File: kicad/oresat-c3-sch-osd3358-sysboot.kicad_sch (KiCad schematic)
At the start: 21 parts, among them J6 Conn_01x02, U1 OSD3358-512M-BSM

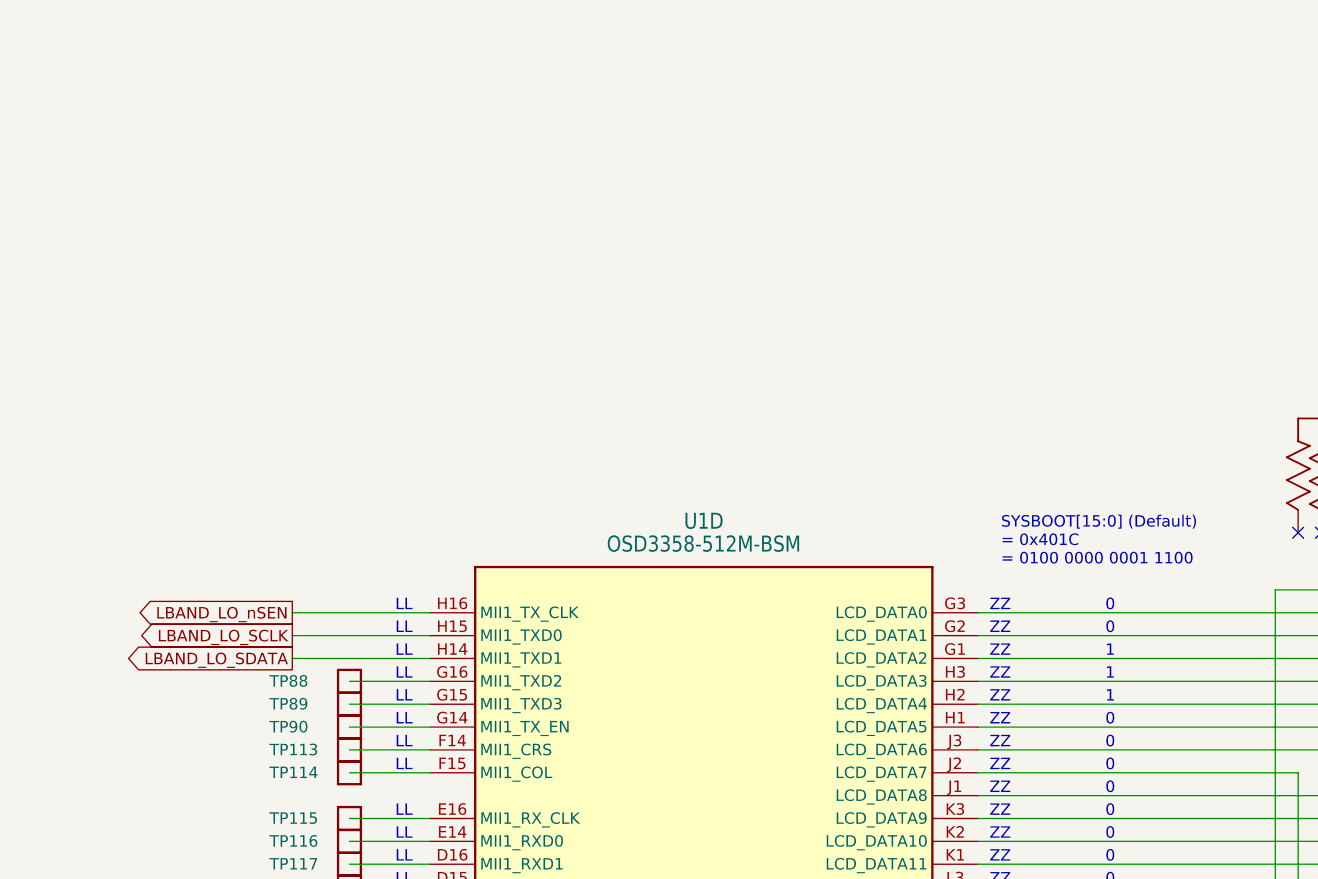
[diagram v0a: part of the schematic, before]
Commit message: Ryan made me do it: added CAN0 tranceiver.
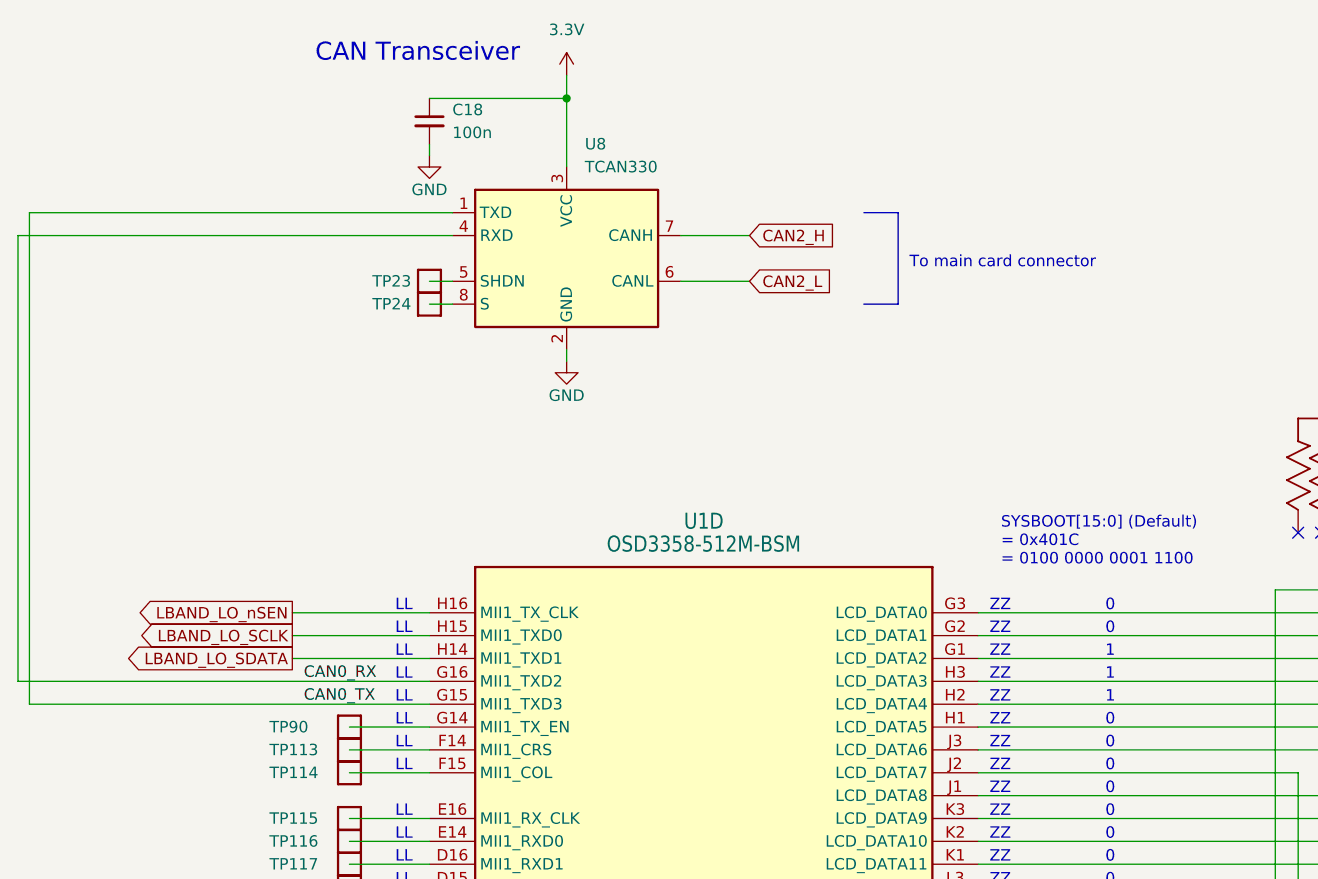
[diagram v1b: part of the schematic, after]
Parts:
- removed TP88, TP89: Test-Point, oresat-misc:TestPoint_Pad_D1.0mm, symbol oresat-misc:Test-Point-1mm-round
- added C18: 100n, Capacitor_SMD:C_0603_1608Metric, symbol Device:C_Small
- added TP23, TP24: Test-Point, oresat-misc:TestPoint_Pad_D1.0mm, symbol oresat-misc:Test-Point-1mm-round
- added U8: TCAN330, Package_TO_SOT_SMD:SOT-23-8, symbol Interface_CAN_LIN:TCAN330
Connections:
- net 3.3V: now also C18.1, U8.3 (VCC)
- net GND: now also C18.2, U8.2 (GND)
- net CAN0_TX: now reaches U1.G15 (MII1_TXD3)
- net CAN0_TX: now also U8.1 (TXD)
- net CAN0_RX: now reaches U1.G16 (MII1_TXD2)
- net CAN0_RX: now also U8.4 (RXD)
- new net: TP23.1, U8.5 (SHDN)
- new net: TP24.1, U8.8 (S)
- new net CAN2_H: U8.7 (CANH)
- new net CAN2_L: U8.6 (CANL)
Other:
- note added: "CAN Transceiver"
- note added: "To main card connector"

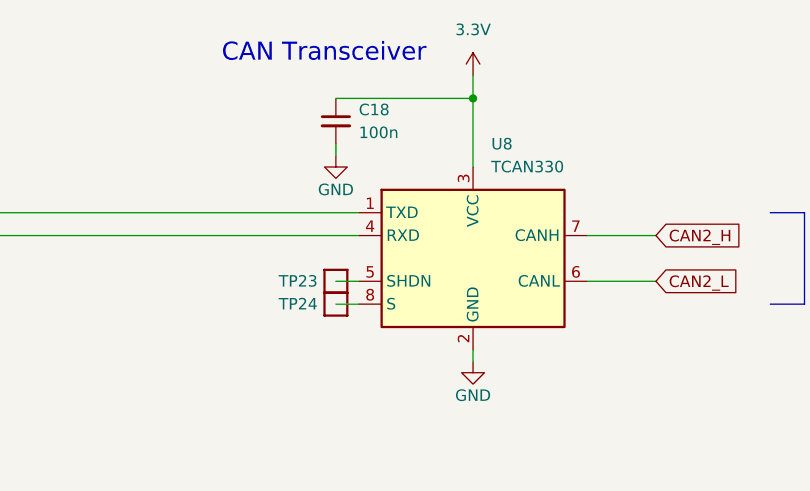
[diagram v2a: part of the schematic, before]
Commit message: Fixed Q1 in the I2C subsystem, which was backward but we never noticed. Removed hardware ID resistors and added back in test points, since HW ID is now stored in internal EEPROM. Updated power measurement values in UHF transmit path. Finally, added circuitry to enable USB lines over the UART backplane. This involves switching the UART signals for the USB signals, and pulling VBUS high to trigger USB on the Octavo. It's pretty janky, so we'll see if it works!
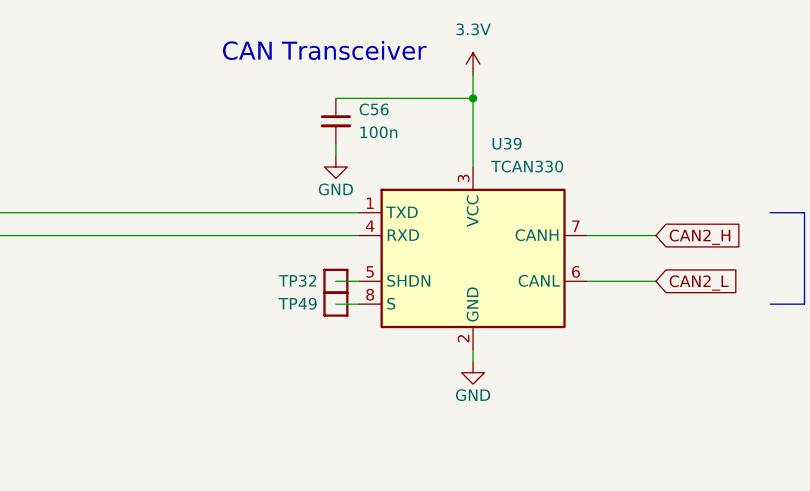
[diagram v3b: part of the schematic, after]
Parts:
- renumbered C18 to C56, TP23 to TP32, TP24 to TP49, U8 to U39
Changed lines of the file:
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@@
   (symbol (lib_id "oresat-power:3.3V") (at 132.08 69.85 0) (unit 1)
     (in_bom yes) (on_board yes) (dnp no) (fields_autoplaced)
-    (property "Reference" "#3V0105" (at 132.08 73.66 0)
+    (property "Reference" "#3V06" (at 132.08 73.66 0)
       (effects (font (size 1.27 1.27)) hide)
     )
@@
     (instances
       (project "oresat-c3"
-        (path "/65d12cdd-c326-4033-9053-c59fa4e0b25e/f3d147ad-4cea-4d77-ae60-95882b03454e"
-          (reference "#3V0105") (unit 1)
-        )
         (path "/65d12cdd-c326-4033-9053-c59fa4e0b25e/0c732c1e-ab0d-41ac-9d77-9d7763333b6f"
           (reference "#3V06") (unit 1)
@@
   (symbol (lib_id "Interface_CAN_LIN:TCAN330") (at 132.08 90.17 0) (unit 1)
     (in_bom yes) (on_board yes) (dnp no) (fields_autoplaced)
-    (property "Reference" "U8" (at 134.0994 77.47 0)
+    (property "Reference" "U39" (at 134.0994 77.47 0)
       (effects (font (size 1.27 1.27)) (justify left))
     )
@@
     (instances
       (project "oresat-c3"
-        (path "/65d12cdd-c326-4033-9053-c59fa4e0b25e/f3d147ad-4cea-4d77-ae60-95882b03454e"
-          (reference "U8") (unit 1)
-        )
         (path "/65d12cdd-c326-4033-9053-c59fa4e0b25e/0c732c1e-ab0d-41ac-9d77-9d7763333b6f"
           (reference "U39") (unit 1)
@@
   (symbol (lib_id "oresat-misc:Test-Point-1mm-round") (at 116.84 92.71 0) (unit 1)
     (in_bom yes) (on_board yes) (dnp no)
-    (property "Reference" "TP23" (at 110.49 92.71 0)
+    (property "Reference" "TP32" (at 110.49 92.71 0)
       (effects (font (size 1.27 1.27)) (justify left))
     )
@@
     (instances
       (project "oresat-c3"
-        (path "/65d12cdd-c326-4033-9053-c59fa4e0b25e/f3d147ad-4cea-4d77-ae60-95882b03454e"
-          (reference "TP23") (unit 1)
-        )
         (path "/65d12cdd-c326-4033-9053-c59fa4e0b25e/0c732c1e-ab0d-41ac-9d77-9d7763333b6f"
           (reference "TP32") (unit 1)
@@
   (symbol (lib_id "Device:C_Small") (at 116.84 74.93 0) (unit 1)
     (in_bom yes) (on_board yes) (dnp no) (fields_autoplaced)
-    (property "Reference" "C18" (at 119.38 73.6662 0)
+    (property "Reference" "C56" (at 119.38 73.6662 0)
       (effects (font (size 1.27 1.27)) (justify left))
     )
@@
     (instances
       (project "oresat-c3"
-        (path "/65d12cdd-c326-4033-9053-c59fa4e0b25e/f3d147ad-4cea-4d77-ae60-95882b03454e"
-          (reference "C18") (unit 1)
-        )
         (path "/65d12cdd-c326-4033-9053-c59fa4e0b25e/0c732c1e-ab0d-41ac-9d77-9d7763333b6f"
           (reference "C56") (unit 1)
@@
   (symbol (lib_id "oresat-misc:Test-Point-1mm-round") (at 116.84 95.25 0) (unit 1)
     (in_bom yes) (on_board yes) (dnp no)
-    (property "Reference" "TP24" (at 110.49 95.25 0)
+    (property "Reference" "TP49" (at 110.49 95.25 0)
       (effects (font (size 1.27 1.27)) (justify left))
     )
@@
     (instances
       (project "oresat-c3"
-        (path "/65d12cdd-c326-4033-9053-c59fa4e0b25e/f3d147ad-4cea-4d77-ae60-95882b03454e"
-          (reference "TP24") (unit 1)
-        )
         (path "/65d12cdd-c326-4033-9053-c59fa4e0b25e/0c732c1e-ab0d-41ac-9d77-9d7763333b6f"
           (reference "TP49") (unit 1)
@@
   (symbol (lib_id "power:GND") (at 132.08 101.6 0) (unit 1)
     (in_bom yes) (on_board yes) (dnp no)
-    (property "Reference" "#PWR0159" (at 132.08 107.95 0)
+    (property "Reference" "#PWR014" (at 132.08 107.95 0)
       (effects (font (size 1.27 1.27)) hide)
     )
@@
     (instances
       (project "oresat-c3"
-        (path "/65d12cdd-c326-4033-9053-c59fa4e0b25e/f3d147ad-4cea-4d77-ae60-95882b03454e"
-          (reference "#PWR0159") (unit 1)
-        )
         (path "/65d12cdd-c326-4033-9053-c59fa4e0b25e/0c732c1e-ab0d-41ac-9d77-9d7763333b6f"
           (reference "#PWR014") (unit 1)
@@
   (symbol (lib_id "power:GND") (at 116.84 78.74 0) (unit 1)
     (in_bom yes) (on_board yes) (dnp no)
-    (property "Reference" "#PWR0156" (at 116.84 85.09 0)
+    (property "Reference" "#PWR013" (at 116.84 85.09 0)
       (effects (font (size 1.27 1.27)) hide)
     )
@@
     (instances
       (project "oresat-c3"
-        (path "/65d12cdd-c326-4033-9053-c59fa4e0b25e/f3d147ad-4cea-4d77-ae60-95882b03454e"
-          (reference "#PWR0156") (unit 1)
-        )
         (path "/65d12cdd-c326-4033-9053-c59fa4e0b25e/0c732c1e-ab0d-41ac-9d77-9d7763333b6f"
           (reference "#PWR013") (unit 1)

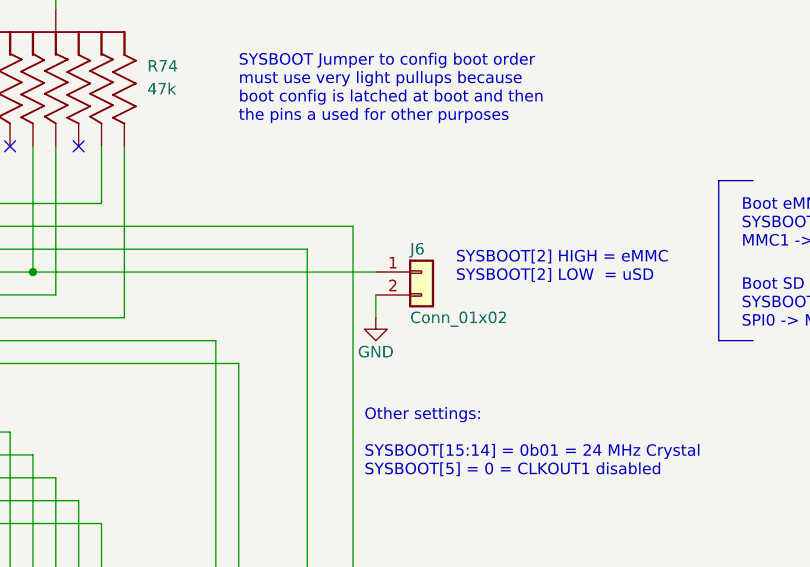
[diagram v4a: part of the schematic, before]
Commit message: BOM cleanups; modified test points to not show up on BOMs, fixed some minor BOM shenaigans (3k vs 3.0k), and imported into the board.
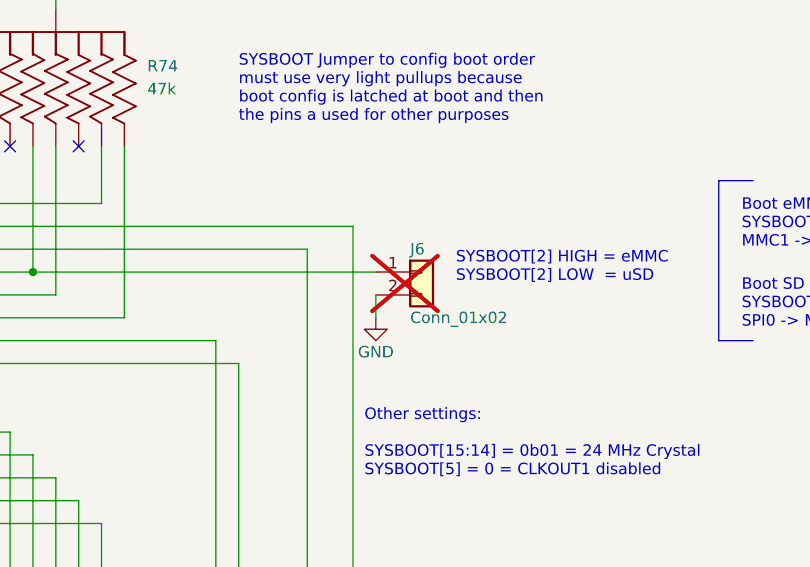
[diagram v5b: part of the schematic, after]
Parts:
- J6: now not fitted
- TP113, TP114, TP115, TP116, TP117, TP118, TP119, TP120, TP121, TP123, TP125, TP134, TP136, TP32, TP49, TP90: now left out of the parts list

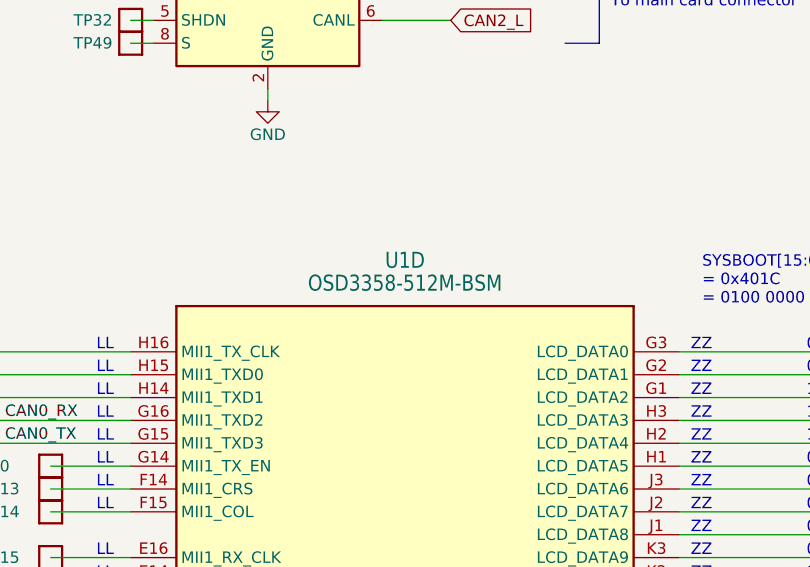
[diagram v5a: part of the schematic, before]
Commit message: Fixed more part numbers while in process of doing BOM inventory, including eMMC and FRAM.
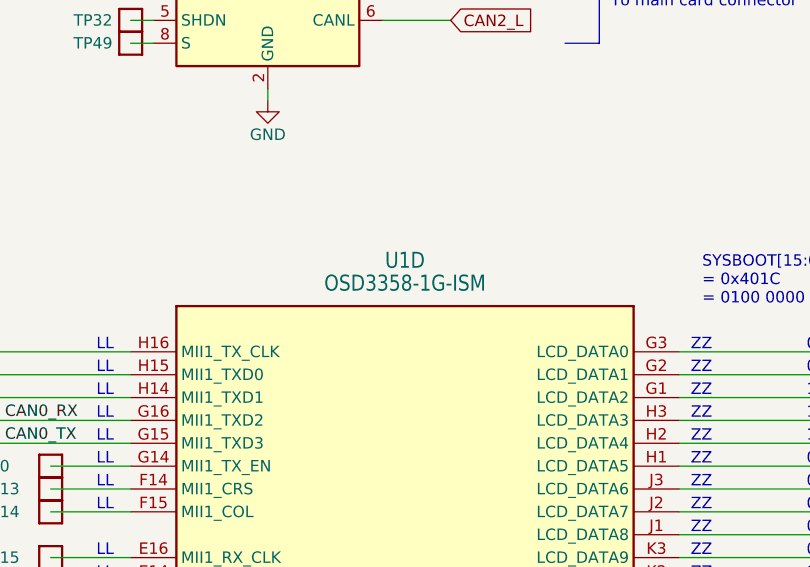
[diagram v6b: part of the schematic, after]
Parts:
- U1: value OSD3358-512M-BSM -> OSD3358-1G-ISM
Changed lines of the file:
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@@
 			)
 		)
-		(property "Value" "OSD3358-512M-BSM"
+		(property "Value" "OSD3358-1G-ISM"
 			(at 147.32 121.92 0)
 			(effects

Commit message: Added MFR, MPN, Description, DST, and DPN to all components using the amazing KiCAD table properties editor. Yay KiCAD. Attemping to make the BOM be self-assembling.
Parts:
- C56: DPN (none) -> 587-3472-1-ND; DST (none) -> Digi-Key; MFR (none) -> Taiyo Yuden; MPN (none) -> TMK107BJ104KAHT
- R72, R73, R74: DPN (none) -> U7473CT-ND; DST (none) -> Digi-Key; MFR (none) -> Panasonic Electronic Components; MPN (none) -> EXB-A10P473J
- U1: DPN (none) -> 1676-OSD3358-1G-ISM-ND; DST (none) -> Digi-Key; Distributor DigiKey -> (none); MFR (none) -> Octavo Systems; MPN OSD3358-512M-BSM -> OSD3358-1G-ISM
- U39: DPN (none) -> 296-44211-1-ND; DST (none) -> Digi-Key; MFR (none) -> Texas Instruments; MPN (none) -> TCAN330GDCNT
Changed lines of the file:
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@@
 			)
 		)
-		(property "Description" ""
+		(property "Description" "47k Ohm ±5% 62.5mW Power Per Element Bussed 8 Resistor Network/Array ±200ppm/°C 2512 (6432 Metric), Concave, Long Side Terminals"
+			(at 256.54 185.42 0)
+			(effects
+				(font
+					(size 1.27 1.27)
+				)
+				(hide yes)
+			)
+		)
+		(property "DPN" "U7473CT-ND"
+			(at 256.54 185.42 0)
+			(effects
+				(font
+					(size 1.27 1.27)
+				)
+				(hide yes)
+			)
+		)
+		(property "DST" "Digi-Key"
+			(at 256.54 185.42 0)
+			(effects
+				(font
+					(size 1.27 1.27)
+				)
+				(hide yes)
+			)
+		)
+		(property "MFR" "Panasonic Electronic Components"
+			(at 256.54 185.42 0)
+			(effects
+				(font
+					(size 1.27 1.27)
+				)
+				(hide yes)
+			)
+		)
+		(property "MPN" "EXB-A10P473J"
 			(at 256.54 185.42 0)
 			(effects
@@
 			)
 		)
-		(property "Description" ""
+		(property "Description" "1/1 Transceiver CANbus SOT-23-8"
+			(at 132.08 90.17 0)
+			(effects
+				(font
+					(size 1.27 1.27)
+				)
+				(hide yes)
+			)
+		)
+		(property "DPN" "296-44211-1-ND"
+			(at 132.08 90.17 0)
+			(effects
+				(font
+					(size 1.27 1.27)
+				)
+				(hide yes)
+			)
+		)
+		(property "DST" "Digi-Key"
+			(at 132.08 90.17 0)
+			(effects
+				(font
+					(size 1.27 1.27)
+				)
+				(hide yes)
+			)
+		)
+		(property "MFR" "Texas Instruments"
+			(at 132.08 90.17 0)
+			(effects
+				(font
+					(size 1.27 1.27)
+				)
+				(hide yes)
+			)
+		)
+		(property "MPN" "TCAN330GDCNT"
 			(at 132.08 90.17 0)
 			(effects
@@
 			)
 		)
-		(property "Description" ""
+		(property "Description" "100 nF (0.1µF) ±10% 25V Ceramic Capacitor X5R 0603 (1608 Metric)"
+			(at 116.84 74.93 0)
+			(effects
+				(font
+					(size 1.27 1.27)
+				)
+				(hide yes)
+			)
+		)
+		(property "DPN" "587-3472-1-ND"
+			(at 116.84 74.93 0)
+			(effects
+				(font
+					(size 1.27 1.27)
+				)
+				(hide yes)
+			)
+		)
+		(property "DST" "Digi-Key"
+			(at 116.84 74.93 0)
+			(effects
+				(font
+					(size 1.27 1.27)
+				)
+				(hide yes)
+			)
+		)
+		(property "MFR" "Taiyo Yuden"
+			(at 116.84 74.93 0)
+			(effects
+				(font
+					(size 1.27 1.27)
+				)
+				(hide yes)
+			)
+		)
+		(property "MPN" "TMK107BJ104KAHT"
 			(at 116.84 74.93 0)
 			(effects
@@
 			)
 		)
-		(property "Description" "OSD335x Embedded Module 1GHz 512MB"
+		(property "Description" "Embedded Module ARM® Cortex®-A8, AM3358 1GHz 1GB"
 			(at 147.32 53.34 0)
 			(effects
@@
 			)
 		)
-		(property "Distributor" "DigiKey"
-			(at 147.32 55.88 0)
-			(effects
-				(font
-					(size 1.27 1.27)
-				)
-				(hide yes)
-			)
-		)
-		(property "MPN" "OSD3358-512M-BSM"
+		(property "MPN" "OSD3358-1G-ISM"
 			(at 147.32 58.42 0)
+			(effects
+				(font
+					(size 1.27 1.27)
+				)
+				(hide yes)
+			)
+		)
+		(property "DPN" "1676-OSD3358-1G-ISM-ND"
+			(at 147.32 157.48 0)
+			(effects
+				(font
+					(size 1.27 1.27)
+				)
+				(hide yes)
+			)
+		)
+		(property "DST" "Digi-Key"
+			(at 147.32 157.48 0)
+			(effects
+				(font
+					(size 1.27 1.27)
+				)
+				(hide yes)
+			)
+		)
+		(property "MFR" "Octavo Systems"
+			(at 147.32 157.48 0)
 			(effects
 				(font
@@
 			)
 		)
-		(property "Description" ""
+		(property "Description" "47k Ohm ±5% 62.5mW Power Per Element Bussed 8 Resistor Network/Array ±200ppm/°C 2512 (6432 Metric), Concave, Long Side Terminals"
+			(at 231.14 185.42 0)
+			(effects
+				(font
+					(size 1.27 1.27)
+				)
+				(hide yes)
+			)
+		)
+		(property "DPN" "U7473CT-ND"
+			(at 231.14 185.42 0)
+			(effects
+				(font
+					(size 1.27 1.27)
+				)
+				(hide yes)
+			)
+		)
+		(property "DST" "Digi-Key"
+			(at 231.14 185.42 0)
+			(effects
+				(font
+					(size 1.27 1.27)
+				)
+				(hide yes)
+			)
+		)
+		(property "MFR" "Panasonic Electronic Components"
+			(at 231.14 185.42 0)
+			(effects
+				(font
+					(size 1.27 1.27)
+				)
+				(hide yes)
+			)
+		)
+		(property "MPN" "EXB-A10P473J"
 			(at 231.14 185.42 0)
 			(effects
@@
 			)
 		)
-		(property "Description" ""
+		(property "Description" "47k Ohm ±5% 62.5mW Power Per Element Bussed 8 Resistor Network/Array ±200ppm/°C 2512 (6432 Metric), Concave, Long Side Terminals"
 			(at 213.36 107.95 0)
 			(effects
+				(font
+					(size 1.27 1.27)
+				)
+				(hide yes)
+			)
+		)
+		(property "DPN" "U7473CT-ND"
+			(at 213.36 107.95 0)
+			(effects
+				(font
+					(size 1.27 1.27)
+				)
+				(hide yes)
+			)
+		)
+		(property "DST" "Digi-Key"
+			(at 213.36 107.95 0)
+			(effects
+				(font
+					(size 1.27 1.27)
+				)
+				(hide yes)
+			)
+		)
+		(property "MFR" "Panasonic Electronic Components"
+			(at 213.36 107.95 0)
+			(effects
+				(font
+					(size 1.27 1.27)
+				)
+				(hide yes)
+			)
+		)
+		(property "MPN" "EXB-A10P473J"
+			(at 213.36 107.95 0)
+			(effects

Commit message: C3 v6.1 release
Updated to KiCad 9.0.6. Updated to version 6.1; there are small changes that have been lost in time. Lots of new ERC and DRC errors that need to be cleaned up.
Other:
- company: (none) -> Portland State Aerospace Society
- title: OreSat C3: OSD3358 SIP D -> OreSat C3 Card
